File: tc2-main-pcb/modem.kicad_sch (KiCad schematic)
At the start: 29 parts, among them J111 Conn_01x08, J112 Screw_Terminal_01x01, U112 TPS62A02DRLR, U116 SIM7600G-H-M.2

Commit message: v0.7.3
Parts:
- J111: now not fitted
- U112: LCSC (none) -> C5350187

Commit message: 0.8.0 WIP
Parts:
- R143, R144, R145: value 22ohm -> 22Ω
- U112: footprint Package_TO_SOT_SMD:SOT-563 -> cacophony-library:SOT-563
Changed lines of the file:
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@@
 	(label "3V8_PHY"
 		(at 132.08 30.48 0)
-		(fields_autoplaced yes)
 		(effects
 			(font
@@
 	(label "3V8_SW"
 		(at 102.87 30.48 0)
-		(fields_autoplaced yes)
 		(effects
 			(font
@@
 	(label "3V8_FB"
 		(at 102.87 40.64 0)
-		(fields_autoplaced yes)
 		(effects
 			(font
@@
 			)
 		)
-		(property "Value" "22ohm"
+		(property "Value" "22Ω"
 			(at 148.59 109.22 90)
 			(effects
@@
 			)
 		)
-		(property "Value" "22ohm"
+		(property "Value" "22Ω"
 			(at 148.59 111.76 90)
 			(effects
@@
 			)
 		)
-		(property "Value" "22ohm"
+		(property "Value" "22Ω"
 			(at 148.59 106.68 90)
 			(effects
@@
 			)
 		)
-		(property "Footprint" "Package_TO_SOT_SMD:SOT-563"
+		(property "Footprint" "cacophony-library:SOT-563"
 			(at 92.71 29.21 0)
 			(effects

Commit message: Updated to use field LCSC Part instead of LCSC for the JLCPCB part number
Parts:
- C135, C138, C155, C156, C157, C160, C161, C162, C172: LCSC C86295 -> (none); LCSC Part (none) -> C86295
- C158, C163: LCSC C16772 -> (none); LCSC Part (none) -> C16772
- C159, C164: LCSC C1547 -> (none); LCSC Part (none) -> C1547
- C176: LCSC C1555 -> (none); LCSC Part (none) -> C1555
- FB103: LCSC C76818 -> (none); LCSC Part (none) -> C76818
- J112: LCSC C2928176 -> (none); LCSC Part (none) -> C2928176
- L104: LCSC C285917 -> (none); LCSC Part (none) -> C285917
- R128, R129, R142: LCSC C25741 -> (none); LCSC Part (none) -> C25741
- R143, R144, R145: LCSC C25092 -> (none); LCSC Part (none) -> C25092
- R162: LCSC C319591 -> (none); LCSC Part (none) -> C319591
- R164: LCSC C445618 -> (none); LCSC Part (none) -> C445618
- U112: LCSC C5350187 -> (none); LCSC Part (none) -> C5350187
- U116: LCSC C2761526 -> (none); LCSC Part (none) -> C2761526
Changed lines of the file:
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@@
 			)
 		)
-		(property "LCSC" "C16772"
+		(property "LCSC Part" "C16772"
 			(at 71.12 92.71 0)
 			(effects
@@
 			)
 		)
-		(property "LCSC" "C25092"
+		(property "LCSC Part" "C25092"
 			(at 142.24 110.49 0)
 			(effects
@@
 			)
 		)
-		(property "LCSC" "C319591"
+		(property "LCSC Part" "C319591"
 			(at 130.81 35.56 0)
 			(effects
@@
 			)
 		)
-		(property "LCSC" "C1547"
+		(property "LCSC Part" "C1547"
 			(at 81.28 92.71 0)
 			(effects
@@
 			)
 		)
-		(property "LCSC" "C86295"
+		(property "LCSC Part" "C86295"
 			(at 40.64 92.71 0)
 			(effects
@@
 			)
 		)
-		(property "LCSC" "C76818"
+		(property "LCSC Part" "C76818"
 			(at 166.37 30.48 0)
 			(effects
@@
 			)
 		)
-		(property "LCSC" "C16772"
+		(property "LCSC Part" "C16772"
 			(at 71.12 113.03 0)
 			(effects
@@
 			)
 		)
-		(property "LCSC" "C86295"
+		(property "LCSC Part" "C86295"
 			(at 50.8 92.71 0)
 			(effects
@@
 			)
 		)
-		(property "LCSC" "C445618"
+		(property "LCSC Part" "C445618"
 			(at 130.81 44.45 0)
 			(effects
@@
 			)
 		)
-		(property "LCSC" "C86295"
+		(property "LCSC Part" "C86295"
 			(at 60.96 113.03 0)
 			(effects
@@
 			)
 		)
-		(property "LCSC" "C86295"
+		(property "LCSC Part" "C86295"
 			(at 43.18 34.29 0)
 			(effects
@@
 			)
 		)
-		(property "LCSC" "C86295"
+		(property "LCSC Part" "C86295"
 			(at 60.96 92.71 0)
 			(effects
@@
 			)
 		)
-		(property "LCSC" "C86295"
+		(property "LCSC Part" "C86295"
 			(at 153.67 35.56 0)
 			(effects
@@
 			)
 		)
-		(property "LCSC" "C86295"
+		(property "LCSC Part" "C86295"
 			(at 33.02 34.29 0)
 			(effects
@@
 			)
 		)
-		(property "LCSC" "C25741"
+		(property "LCSC Part" "C25741"
 			(at 130.81 54.61 0)
 			(effects
@@
 			)
 		)
-		(property "LCSC" "C25092"
+		(property "LCSC Part" "C25092"
 			(at 142.24 113.03 0)
 			(effects
@@
 			)
 		)
-		(property "LCSC" "C25092"
+		(property "LCSC Part" "C25092"
 			(at 142.24 107.95 0)
 			(effects
@@
 			)
 		)
-		(property "LCSC" "C86295"
+		(property "LCSC Part" "C86295"
 			(at 40.64 113.03 0)
 			(effects
@@
 			)
 		)
-		(property "LCSC" "C5350187"
+		(property "LCSC Part" "C5350187"
 			(at 92.71 29.21 0)
 			(effects
@@
 			)
 		)
-		(property "LCSC" "C25741"
+		(property "LCSC Part" "C25741"
 			(at 134.62 83.82 0)
 			(effects
@@
 			)
 		)
-		(property "LCSC" "C285917"
+		(property "LCSC Part" "C285917"
 			(at 123.19 30.48 0)
 			(effects
@@
 			)
 		)
-		(property "LCSC" "C25741"
+		(property "LCSC Part" "C25741"
 			(at 77.47 38.1 0)
 			(effects
@@
 			)
 		)
-		(property "LCSC" "C86295"
+		(property "LCSC Part" "C86295"
 			(at 50.8 113.03 0)
 			(effects
@@
 			)
 		)
-		(property "LCSC" "C2928176"
+		(property "LCSC Part" "C2928176"
 			(at 162.56 148.59 0)
 			(effects
@@
 			)
 		)
-		(property "LCSC" "C1555"
+		(property "LCSC Part" "C1555"
 			(at 142.24 39.37 0)
 			(effects
@@
 			)
 		)
-		(property "LCSC" "C1547"
+		(property "LCSC Part" "C1547"
 			(at 81.28 113.03 0)
 			(effects
@@
 			)
 		)
-		(property "LCSC" "C2761526"
+		(property "LCSC Part" "C2761526"
 			(at 107.95 86.36 0)
 			(effects

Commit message: Tidy up
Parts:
- J111: LCSC Part (none) -> C27438; now fitted; now in the parts list
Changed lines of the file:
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@@
 		(unit 1)
 		(exclude_from_sim no)
-		(in_bom no)
+		(in_bom yes)
 		(on_board yes)
-		(dnp yes)
+		(dnp no)
 		(property "Reference" "J111"
 			(at 193.04 88.9 0)
@@
 			(at 195.58 102.87 0)
 			(effects
+				(font
+					(size 1.27 1.27)
+				)
+				(hide yes)
+			)
+		)
+		(property "LCSC Part" "C27438"
+			(at 195.58 102.87 0)
+			(effects

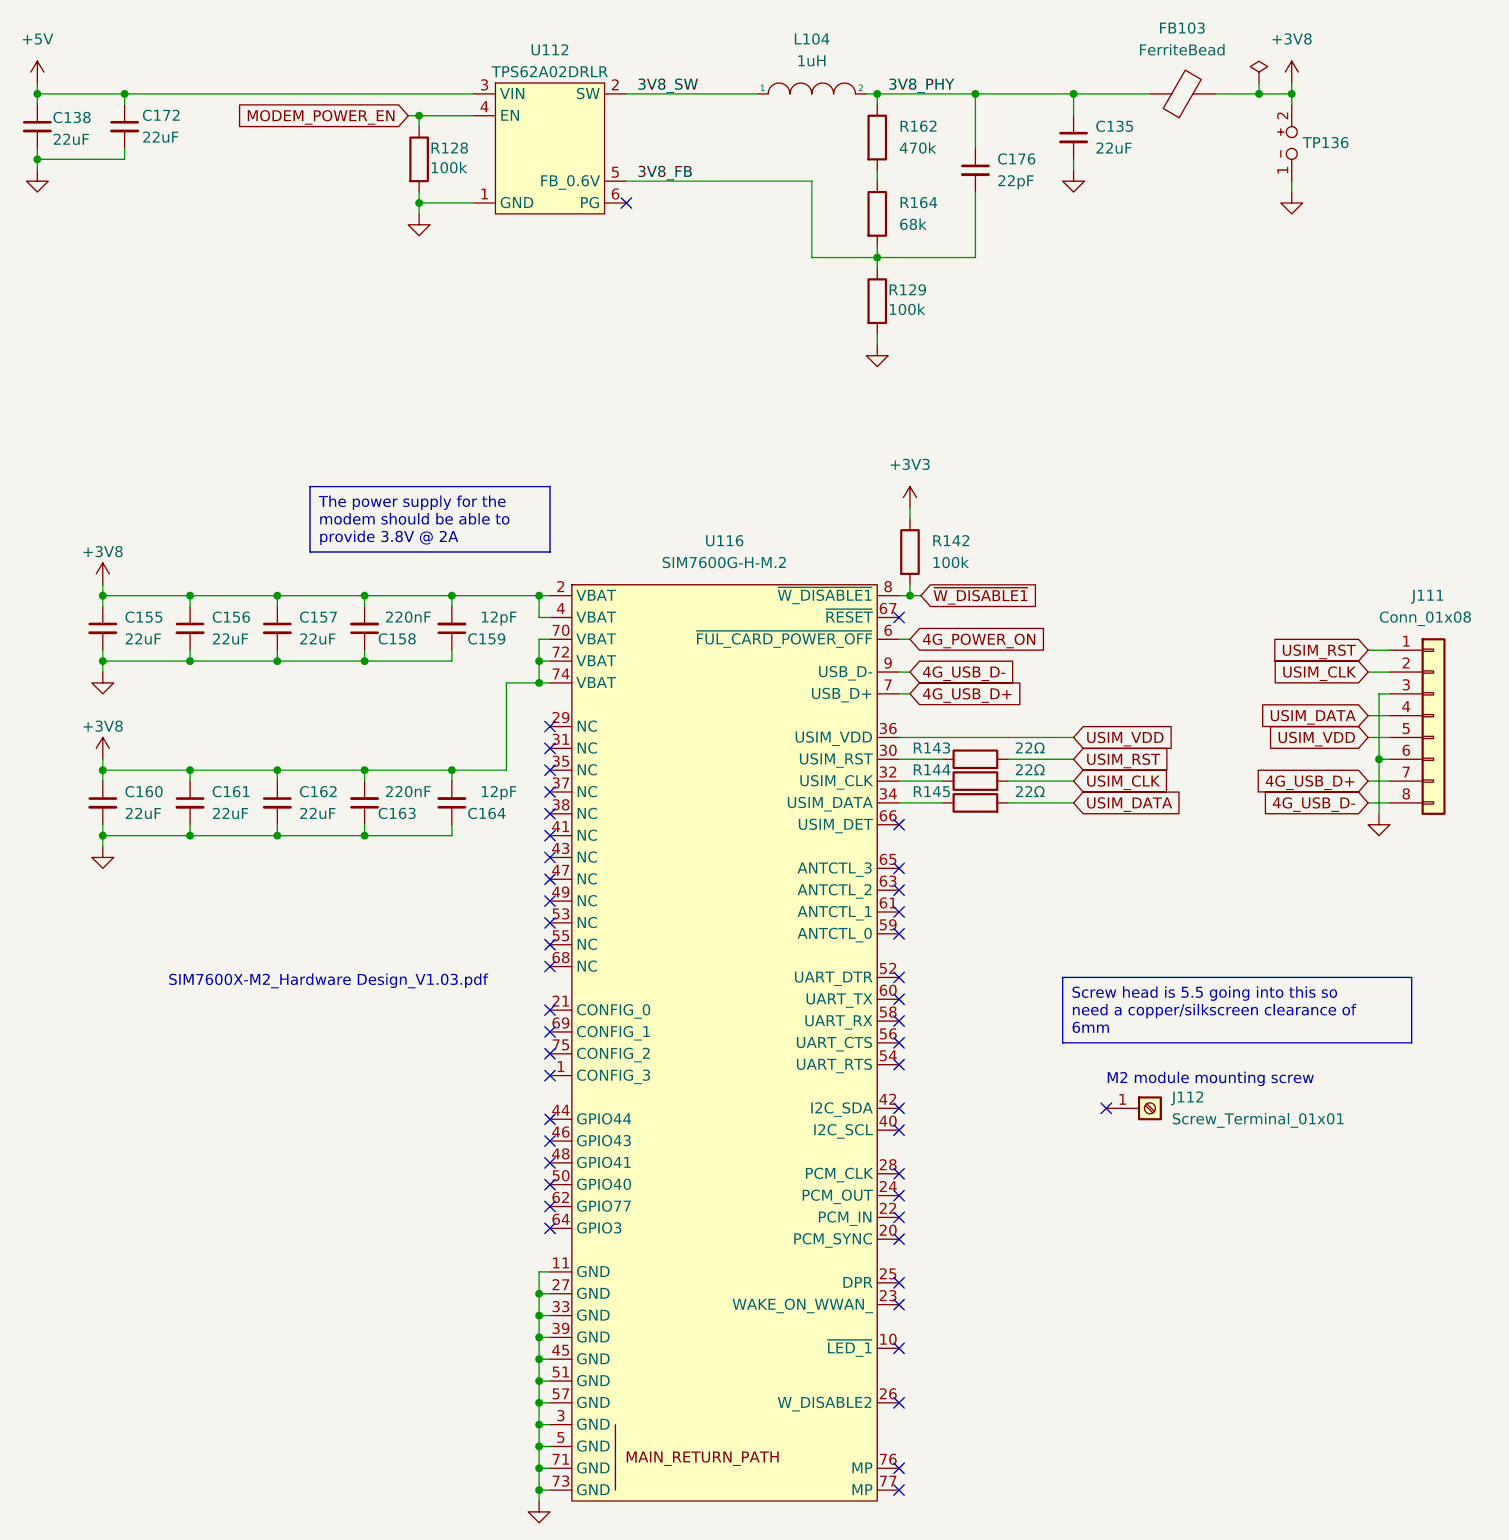
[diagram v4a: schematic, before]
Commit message: Update to kicad 9, fix microphone panel v cuts
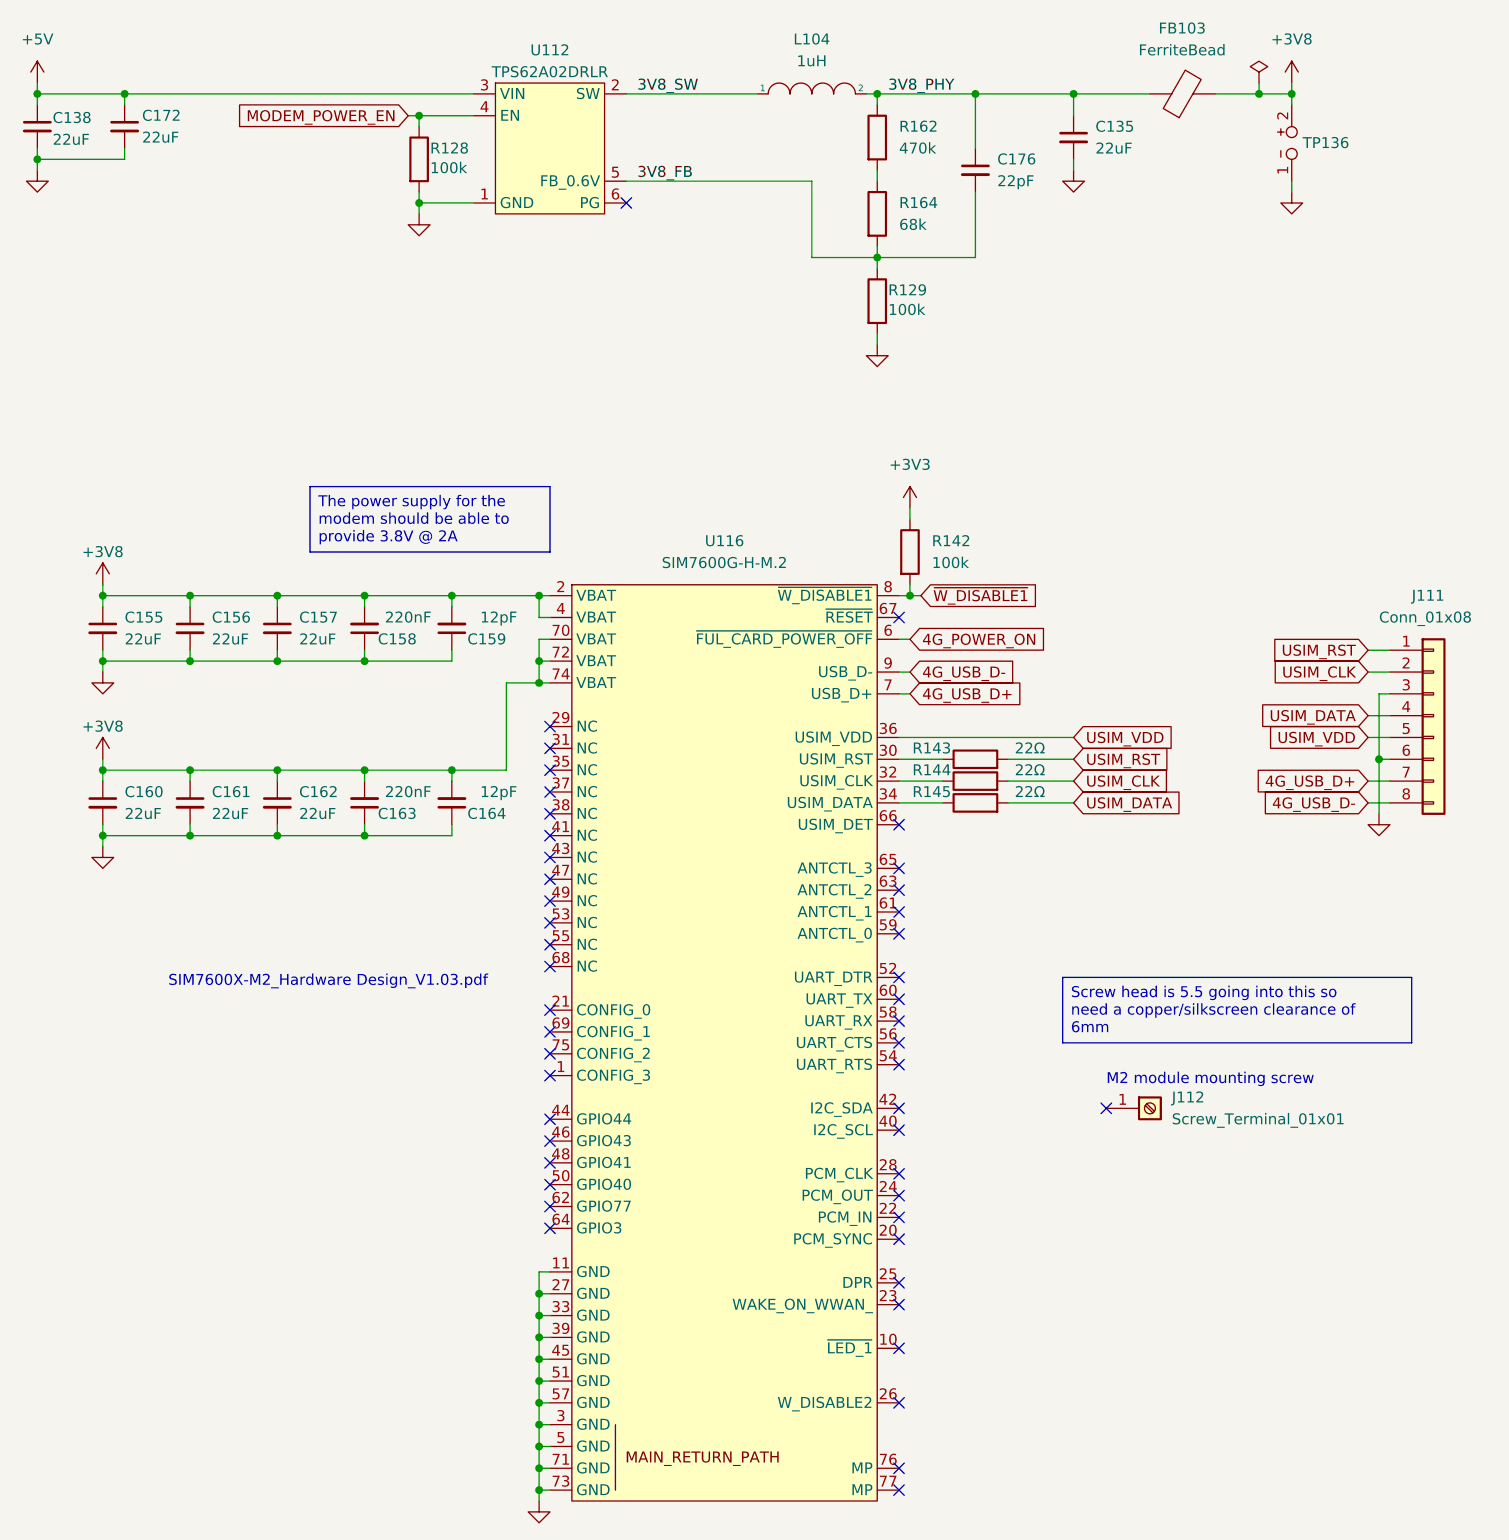
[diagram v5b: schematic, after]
